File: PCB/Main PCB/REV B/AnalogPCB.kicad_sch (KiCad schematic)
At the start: 60 parts, among them J1 DF12NB_4.0_-20DP-0.5V_51_, J2 393570002, J3 393570002, J4 393570002, J5 393570002, J6 Conn_01x03_Female, Q1 2N7002, Q2 2N7002, Q3 2N7002, U1 ALDP105W, U2 ALDP105W, U3 ALDP105W, U4 TS5A23159DGS

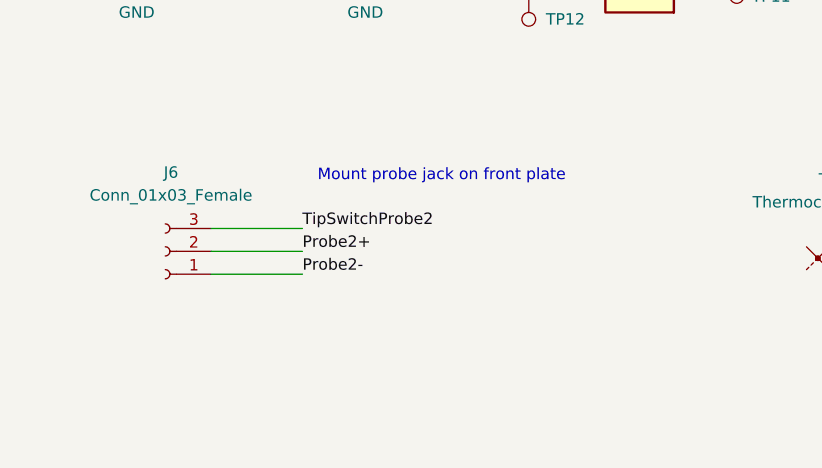
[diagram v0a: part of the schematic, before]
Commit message: PCB - Rough Analog Layout
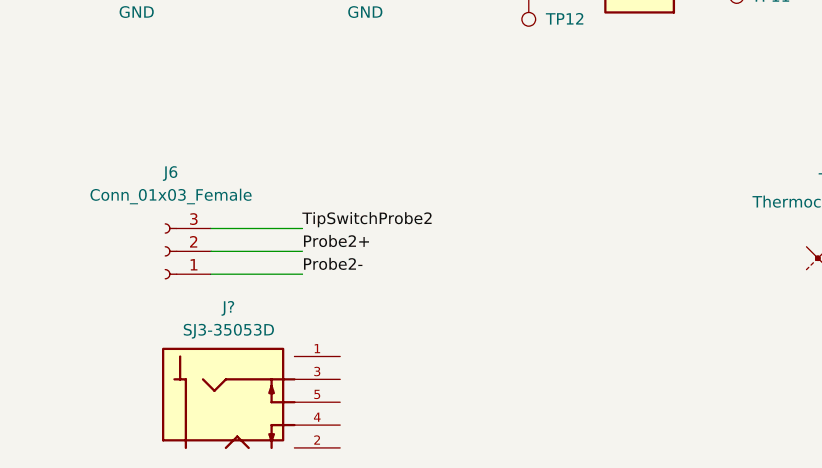
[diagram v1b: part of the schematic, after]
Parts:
- added J?: SJ3-35053D, Customs Smoker:SAMESKY_SJ3-35053D, symbol SJ3-35053D:SJ3-35053D
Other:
- note removed: "Mount probe jack on front plate"
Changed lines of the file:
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@@
     (effects (font (size 3 3) (thickness 1.016) bold) (justify left bottom))
-  )
-  (text "Mount probe jack on front plate\n" (at 53.4924 250.063 0)
-    (effects (font (size 1.27 1.27)) (justify left bottom))
   )
   (text "AC-DC MAIN" (at 52.197 21.844 0)
@@
     )
     (pin "1")
+  )
+  (symbol (lib_id "SJ3-35053D:SJ3-35053D") (at 43.307 274.447 0) (unit 1)
+    (in_bom yes) (on_board yes) (fields_autoplaced)
+    (property "Reference" "J?" (id 0) (at 43.632 263.906 0))
+    (property "Value" "SJ3-35053D" (id 1) (at 43.632 266.446 0))
+    (property "Footprint" "Customs Smoker:SAMESKY_SJ3-35053D" (id 2) (at 43.307 274.447 0)
+      (effects (font (size 1.27 1.27)) (justify bottom) hide)
+    )
+    (property "Datasheet" "" (id 3) (at 43.307 274.447 0)
+      (effects (font (size 1.27 1.27)) hide)
+    )
+    (property "Manufacturer" "SameSky" (id 4) (at 43.307 274.447 0)
+      (effects (font (size 1.27 1.27)) hide)
+    )
+    (property "Manufacturer Part Number" "SJ3-35053D" (id 5) (at 43.307 274.447 0)
+      (effects (font (size 1.27 1.27)) hide)
+    )
+    (property "Vendor" "Digkey" (id 6) (at 43.307 274.447 0)
+      (effects (font (size 1.27 1.27)) hide)
+    )
+    (property "Vendor Part Number" "2223-SJ3-35053D-ND" (id 7) (at 43.307 274.447 0)
+      (effects (font (size 1.27 1.27)) hide)
+    )
+    (pin "1")
+    (pin "2")
+    (pin "3")
+    (pin "4")
+    (pin "5")
   )
   (symbol (lib_id "power:GND") (at 358.394 198.755 0) (mirror y) (unit 1)
@@
       (reference "J6") (unit 1) (value "Conn_01x03_Female") (footprint "Connector_PinHeader_2.54mm:PinHeader_1x03_P2.54mm_Vertical")
     )
+    (path "/01e6dd54-1030-4824-bd57-6df5cdd2ac30"
+      (reference "J?") (unit 1) (value "SJ3-35053D") (footprint "Customs Smoker:SAMESKY_SJ3-35053D")
+    )
     (path "/43fe162c-a537-45fa-a7fc-e4118ef90edc"

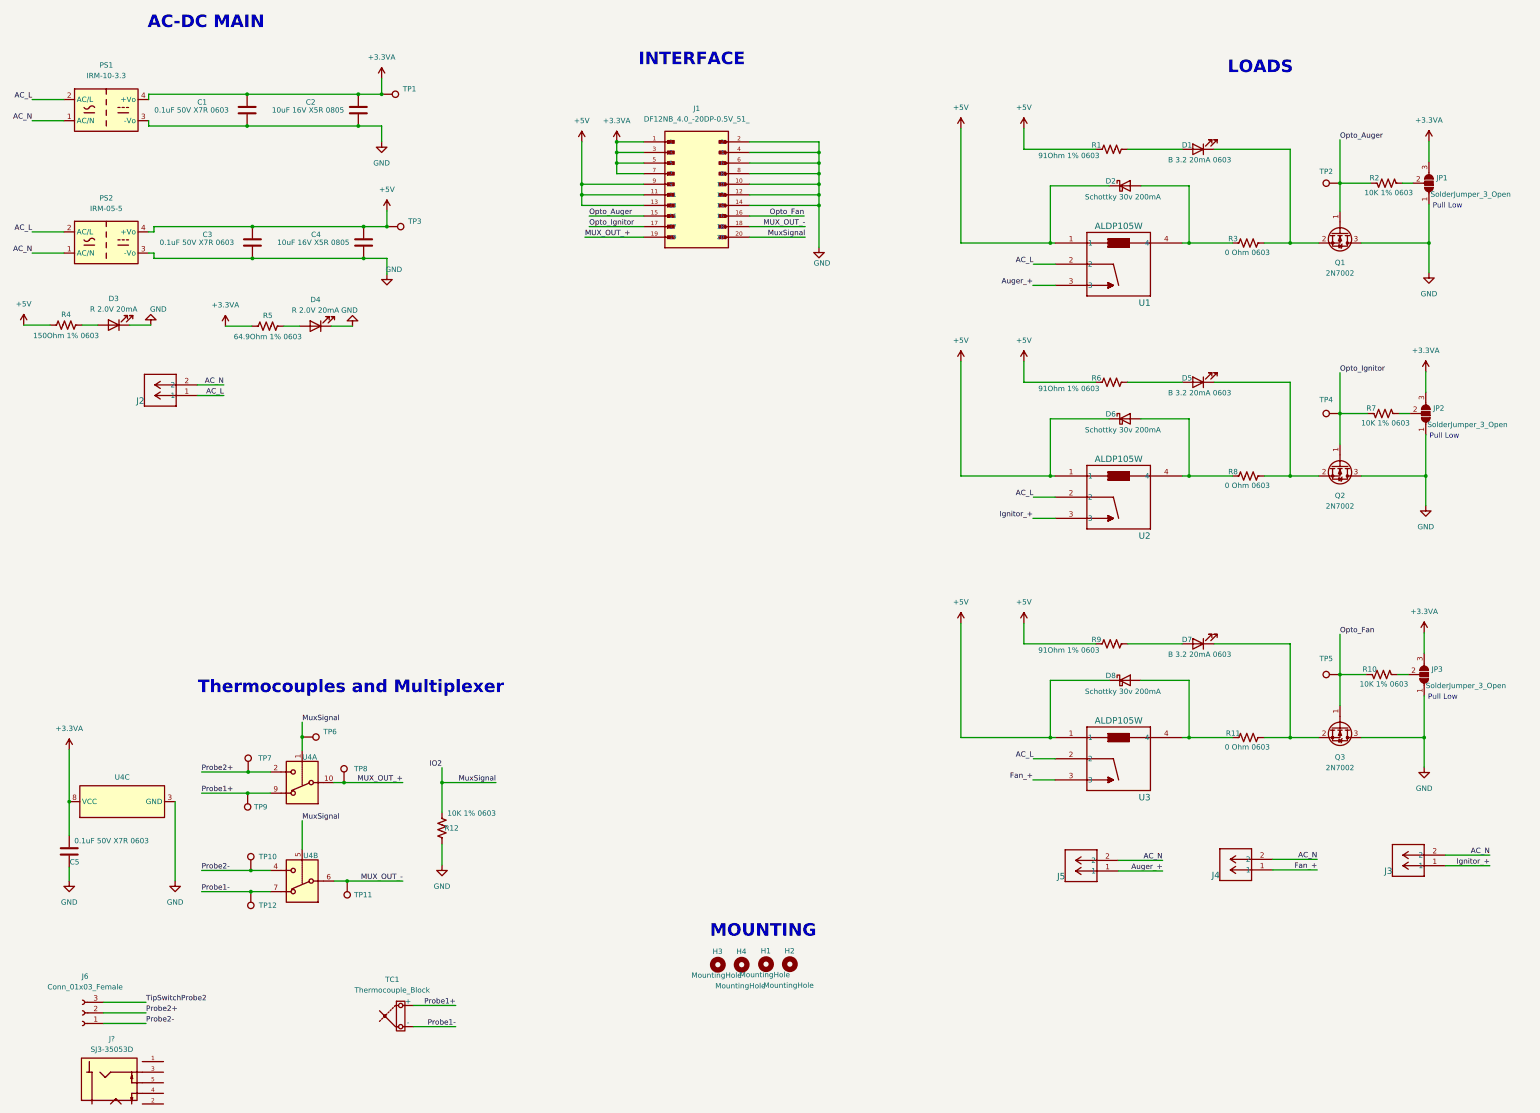
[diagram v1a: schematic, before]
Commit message: PCB - Rough Analog Layout and probe jack change to RTD
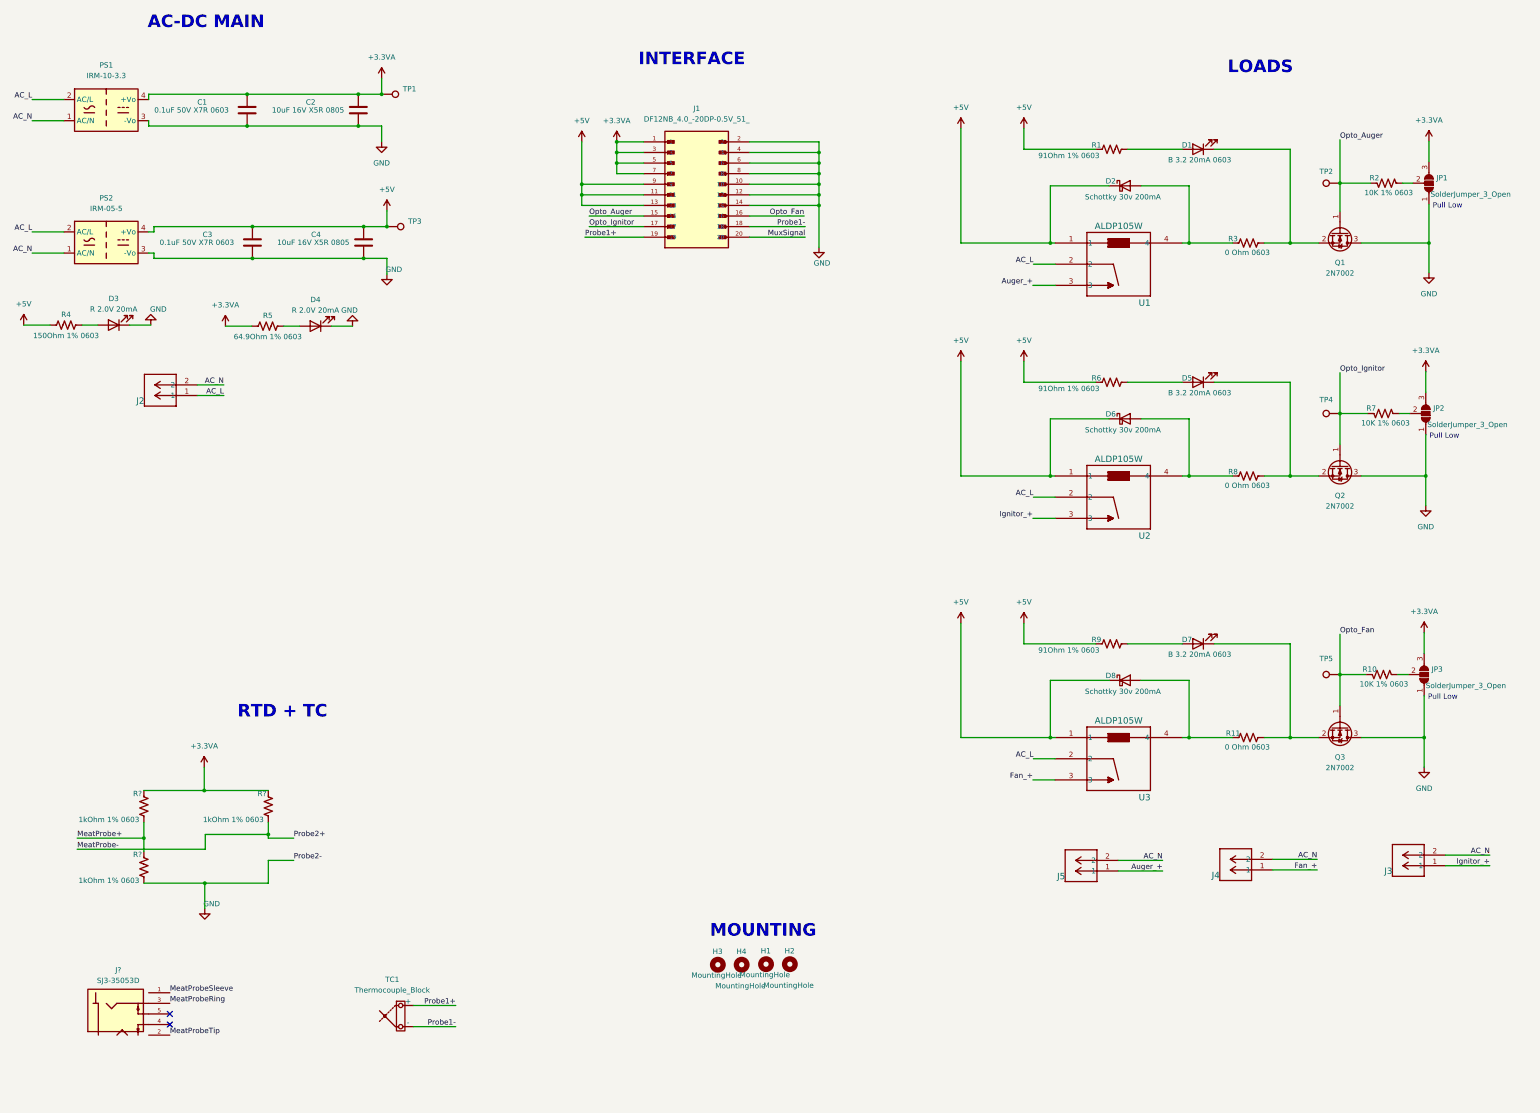
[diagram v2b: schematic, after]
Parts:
- removed C5: 0.1uF 50V X7R 0603, Capacitor_SMD:C_0603_1608Metric, symbol Device:C
- removed J6: Conn_01x03_Female, Connector_PinHeader_2.54mm:PinHeader_1x03_P2.54mm_Vertical, symbol Connector:Conn_01x03_Female
- removed R12: 10K 1% 0603, Resistor_SMD:R_0603_1608Metric, symbol Device:R_US
- removed TP10, TP11, TP12, TP6, TP7, TP8, TP9: TP, TestPoint:TestPoint_Pad_D1.0mm, symbol Connector:TestPoint
- removed U4: TS5A23159DGS, Package_SO:VSSOP-10_3x3mm_P0.5mm, symbol Analog_Switch:TS5A23159DGS
- added R? (x3): 1kOhm 1% 0603, Resistor_SMD:R_0603_1608Metric, symbol Device:R_US
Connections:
- net MUX_OUT_+ is gone; now on net Probe1+: J1.19
- net MUX_OUT_- is gone; now on net Probe1-: J1.18
- net +3.3VA: now also R?.1, R?.1
- net GND: now also R?.2
- net MeatProbeSleeve: now reaches J?.1
- net MeatProbeTip: now reaches J?.2
- net MeatProbeRing: now reaches J?.3
- net IO2 renamed MuxSignal
- new net MeatProbe+: R?.1, R?.2
- new net MeatProbe-: R?.2
- no-connect marks 0 -> 2
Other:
- note added: "RTD + TC"
- note removed: "Thermocouples and Multiplexer"
- moved on the sheet: J?
